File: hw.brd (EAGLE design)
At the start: 80 x 81.3 mm, 37 parts, among them IC1 MIC_I2S_SPH0645, Q3 DMG3415U, U1 MAX98357A, U2 AP2112-3.3, U3 MCP73831T-2ACI/OT, X2 JSTPH

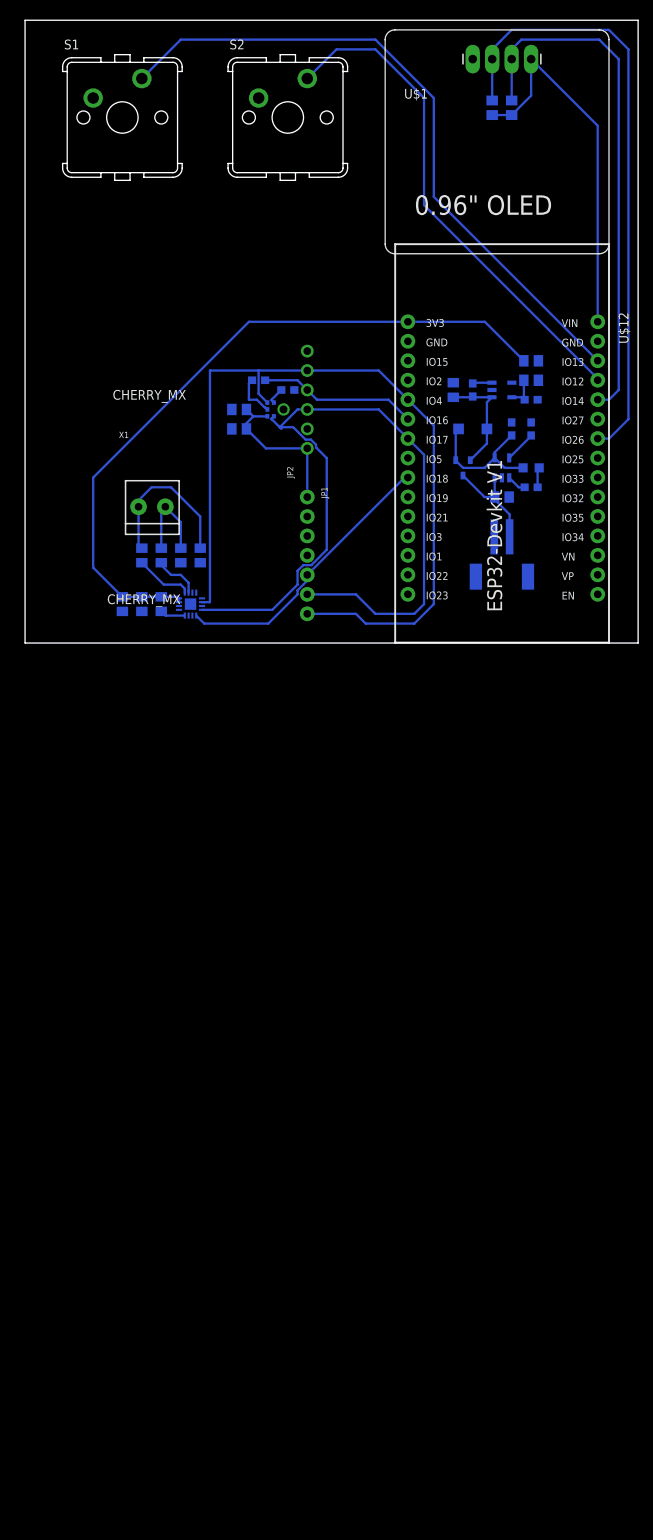
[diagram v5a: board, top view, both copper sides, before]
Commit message: reducing pcb size
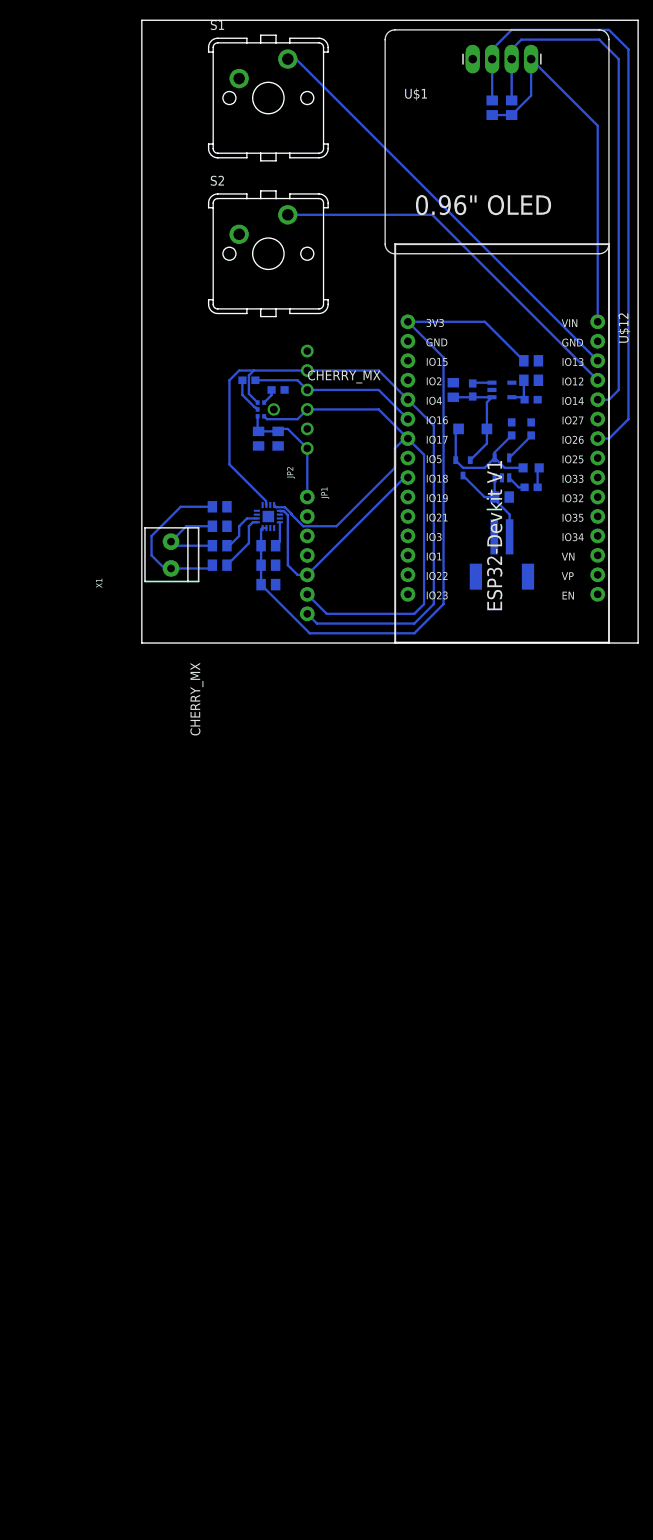
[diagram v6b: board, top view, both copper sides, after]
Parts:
- moved S1 19.2 mm to (31.8, 71.1)
- moved C2 19.2 mm to (31.8, 7.62), turned to 180 degrees
- moved S2 18.0 mm to (31.8, 50.8)
- moved C1 17.3 mm to (31.8, 10.2), turned to 180 degrees
- moved R1 15.9 mm to (31.8, 12.7), turned to 0 degrees
- moved U1 15.3 mm to (31.8, 16.5), turned to 0 degrees
- moved FB1 10.2 mm to (25.4, 10.2), turned to 0 degrees
- moved FB2 7.73 mm to (25.4, 12.7), turned to 0 degrees
- moved C5 6.84 mm to (25.4, 17.8), turned to 180 degrees
- moved X1 6.84 mm to (19.1, 11.4), turned to 90 degrees
- moved C4 6.35 mm to (25.4, 15.2), turned to 180 degrees
- moved C6 5.24 mm to (33.0, 26.7), turned to 270 degrees
- moved C3 4.58 mm to (30.5, 26.7), turned to 270 degrees
- moved IC1 1.27 mm to (31.8, 30.5)
- moved R2 1.27 mm to (29.2, 34.3)
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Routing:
- net BTN2: track 86.5 -> 56.7 mm
- net BCLK: track 101.8 -> 85.2 mm
- net BTN1: track 65.7 -> 49.4 mm
- net LRCLK: track 109.5 -> 94.8 mm
- net DIN: track 36.7 -> 29.3 mm
- net 3.3V: track 116.7 -> 112.6 mm
- net DOUT: track 20.7 -> 22.0 mm
- net N$1: track 5.65 -> 4.69 mm
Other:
- board size 80 x 81.3 mm -> 64.8 x 81.3 mm

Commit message: touch ups before ground plane
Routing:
- net 3.3V: track 112.6 -> 144.8 mm, vias 0 -> 2
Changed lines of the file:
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@@
 <contactref element="IC1" pad="1"/>
 <wire x1="30.35" y1="31.38" x2="29.21" y2="32.52" width="0.3048" layer="16"/>
-<wire x1="49.54" y1="29.21" x2="49.53" y2="29.22" width="0.3048" layer="16"/>
 <wire x1="53.34" y1="5.08" x2="50.8" y2="2.54" width="0.3048" layer="16"/>
 <wire x1="53.34" y1="5.08" x2="53.34" y2="28.38" width="0.3048" layer="16"/>
@@
 <wire x1="26.67" y1="34.29" x2="27.94" y2="35.56" width="0.3048" layer="16"/>
 <wire x1="27.94" y1="35.56" x2="29.86145" y2="35.56" width="0.3048" layer="16"/>
-<wire x1="49.96" y1="31.76" x2="49.54" y2="29.21" width="0" layer="19" extent="16-16"/>
 </signal>
 <signal name="DIN">
@@
 <wire x1="30.48" y1="27.62" x2="30.35" y2="27.75" width="0.3048" layer="16"/>
 <wire x1="30.35" y1="27.75" x2="30.35" y2="29.58" width="0.3048" layer="16"/>
-<wire x1="65.09" y1="36.83" x2="65.09" y2="34.29" width="0" layer="19" extent="16-16"/>
-<wire x1="36.83" y1="19.05" x2="31.5" y2="15.01" width="0" layer="19" extent="16-16"/>
+<wire x1="49.96" y1="41.92" x2="49.95" y2="41.91" width="0.3048" layer="16"/>
+<wire x1="49.95" y1="41.91" x2="45.72" y2="41.91" width="0.3048" layer="16"/>
+<wire x1="36.83" y1="25.4" x2="45.72" y2="25.4" width="0.3048" layer="16"/>
+<via x="45.72" y="25.4" extent="1-16" drill="0.35"/>
+<via x="45.72" y="41.91" extent="1-16" drill="0.35"/>
+<wire x1="45.72" y1="41.91" x2="45.72" y2="25.4" width="0.3048" layer="1"/>
+<wire x1="65.09" y1="34.29" x2="65.09" y2="36.83" width="0.3048" layer="16"/>
 </signal>
 <signal name="EN">

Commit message: some more adjustements for better coverage
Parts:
- moved X1 1.27 mm to (20.3, 11.4)
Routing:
- net GND: track 0.00 -> 22.6 mm
- net VO-: track 11.9 -> 9.31 mm
- net BCLK: track 85.2 -> 83.4 mm
- net LRCLK: track 94.8 -> 93.0 mm
- net 3.3V: track 144.8 -> 143.7 mm
- net VO+: track 20.9 -> 19.8 mm
